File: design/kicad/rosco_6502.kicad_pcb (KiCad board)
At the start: 4 copper layers, 100 x 100 mm, 52 parts, among them IC1 W65C02SxP, IC2 ATF22V10C-7PX, IC3 XR68C681CJTR-F, IC4 NE555P, IC5 ATF22V10C-7PX, J1 UART_A, J2 UART_B, J3 Conn_01x06, J4 Conn_01x01_Male, J5 Conn_02x18_Odd_Even, Q1 3.6864MHz, SW1 SW_DPST, U1 AS6C4008-55PCN, U2 AS6C62256-55PCN, U3 AT28C64B-15PU, U4 74HCT174, X1 14MHz

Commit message: Tidy up some tracks
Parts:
- moved R10 1.33 mm to (98.5, 113.8)
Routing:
- net A12: track 181.7 -> 191.3 mm
- net Net-(IC3-Pad16): track 39.5 -> 46.9 mm
- net Net-(IC3-Pad15): track 48.6 -> 53.9 mm
- net CLK: track 161.8 -> 166.7 mm
- net A8: track 181.1 -> 185.7 mm
- net A13: track 162.7 -> 167.3 mm
- net A14: track 101.4 -> 105.9 mm
- net D2: track 180.4 -> 184.1 mm
- net ~{RESET}: track 235.7 -> 239.3 mm
- net A11: track 172.9 -> 175.0 mm
- net RDY: track 182.5 -> 184.1 mm
- net ~{DUASEL}: track 50.1 -> 48.9 mm
- net D4: track 130.3 -> 131.2 mm
- net D6: track 126.4 -> 127.4 mm
- net D7: track 133.7 -> 132.9 mm
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
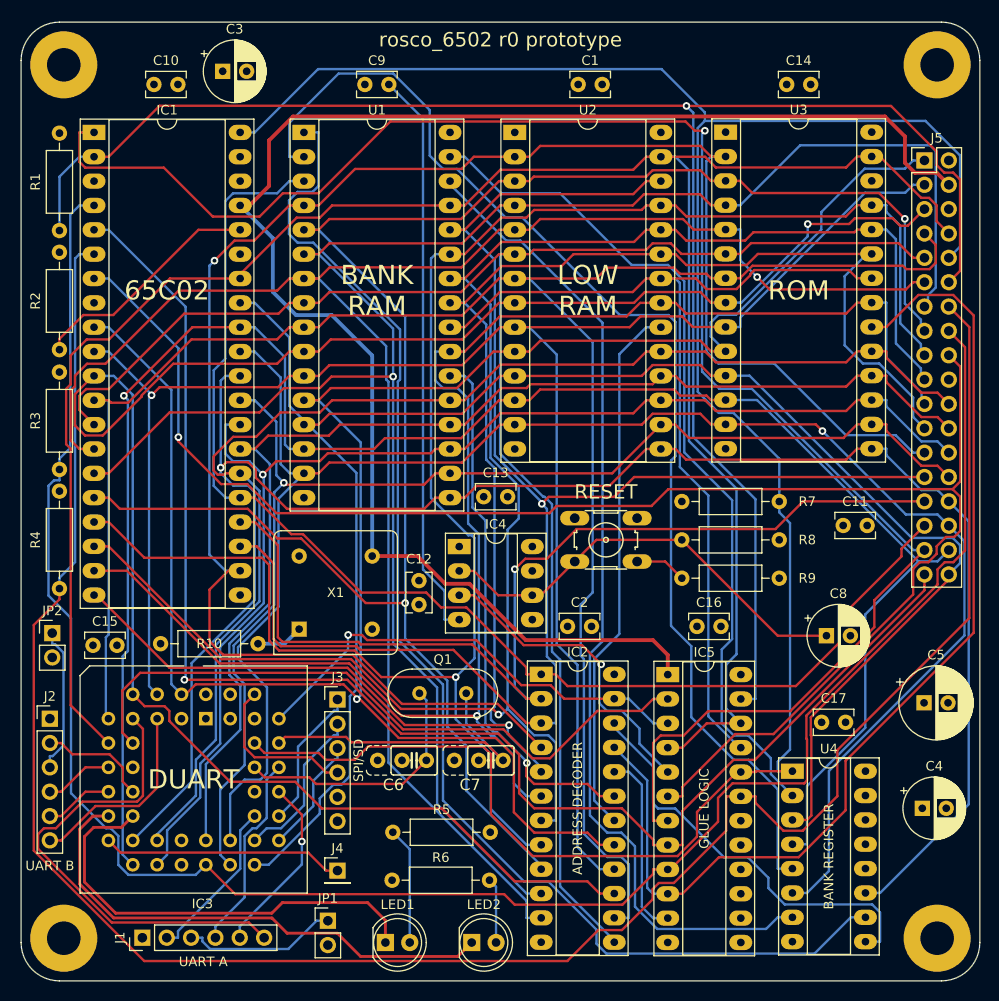
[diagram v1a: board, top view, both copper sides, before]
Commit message: Power connector & silk update
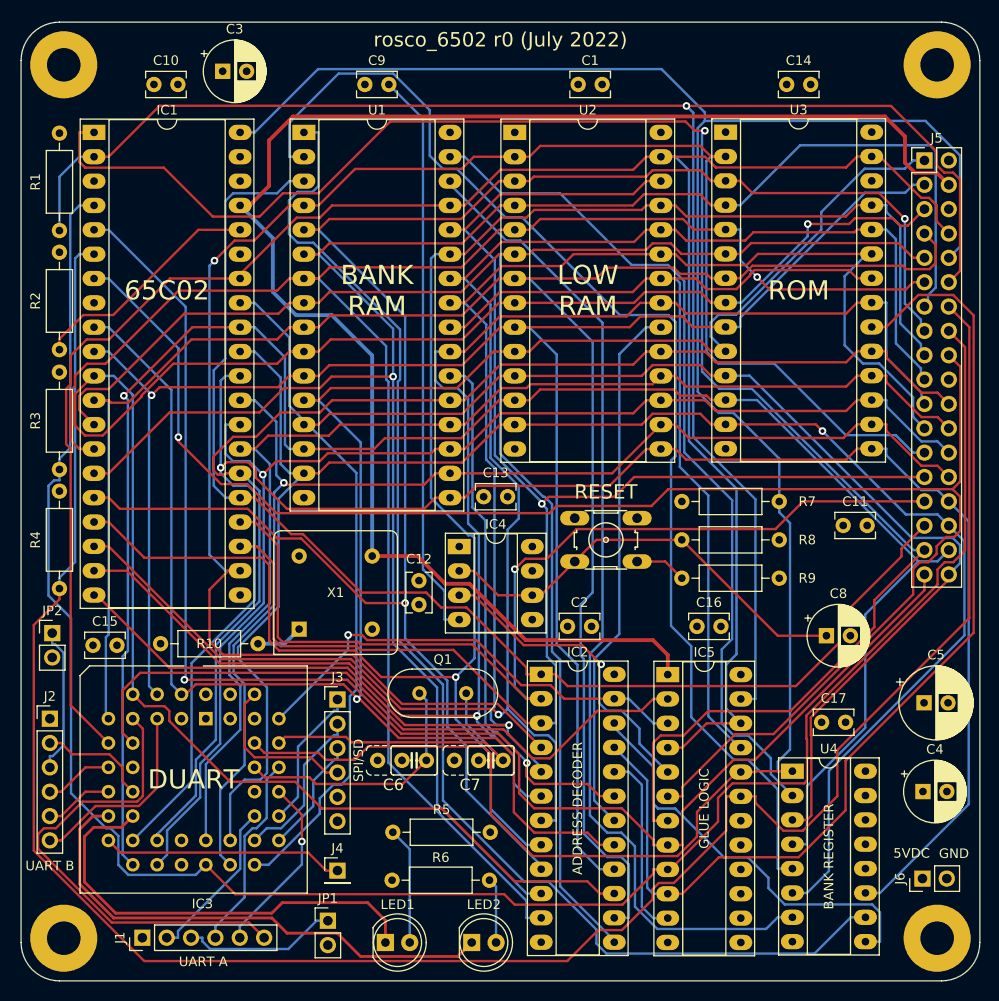
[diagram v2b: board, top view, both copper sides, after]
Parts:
- added J6: Conn_01x02_Male, Connector_PinHeader_2.54mm:PinHeader_1x02_P2.54mm_Vertical, F.Cu at (178.0, 138.3)
- moved C4 1.75 mm to (178.1, 129.2)
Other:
- board text added: "5VDC"
- board text added: "GND"
- board text added: "rosco_6502 r0 (July 2022)"
- board text removed: "rosco_6502 r0 prototype"
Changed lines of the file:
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@@
   )
   (paper "A4")
+  (title_block
+    (title "rosco_6502")
+    (date "2022-06-19")
+    (rev "0")
+    (company "The Really Old-School Company Limited")
+    (comment 1 "Copyright (c)2022 Ross Bamford & Contributors")
+    (comment 2 "Open Source Hardware (CERN OHL)")
+  )
   (layers
     (0 "F.Cu" signal)
@@
       (outputformat 1)
       (mirror false)
-      (drillshape 1)
+      (drillshape 0)
       (scaleselection 1)
-      (outputdirectory "")
+      (outputdirectory "../CAMOutputs/")
     )
   )
@@
   )
   (footprint "Capacitor_THT:CP_Radial_D6.3mm_P2.50mm" (layer "F.Cu")
-    (at 178 131)
+    (at 178.067621 129.25)
     (descr "CP, Radial series, Radial, pin pitch=2.50mm, , diameter=6.3mm, Electrolytic Capacitor")
     (tags "CP Radial series Radial pin pitch 2.50mm  diameter 6.3mm Electrolytic Capacitor")
@@
     )
   )
+  (footprint "Connector_PinHeader_2.54mm:PinHeader_1x02_P2.54mm_Vertical" (layer "F.Cu")
+    (at 178.015 138.33 90)
+    (descr "Through hole straight pin header, 1x02, 2.54mm pitch, single row")
+    (tags "Through hole pin header THT 1x02 2.54mm single row")
+    (property "Sheetfile" "rosco_6502.kicad_sch")
+    (property "Sheetname" "")
+    (attr through_hole)
+    (fp_text reference "J6" (at 0 -2.33 90) (layer "F.SilkS")
+      (effects (font (size 1 1) (thickness 0.15)))
+    )
+    (fp_text value "Conn_01x02_Male" (at 0 4.87 90) (layer "F.Fab")
+      (effects (font (size 1 1) (thickness 0.15)))
+    )
+    (fp_text user "${REFERENCE}" (at 0 1.27) (layer "F.Fab")
+      (effects (font (size 1 1) (thickness 0.15)))
+    )
+    (fp_line (start -1.33 3.87) (end 1.33 3.87) (layer "F.SilkS") (width 0.12))
+    (fp_line (start 1.33 1.27) (end 1.33 3.87) (layer "F.SilkS") (width 0.12))
+    (fp_line (start -1.33 1.27) (end -1.33 3.87) (layer "F.SilkS") (width 0.12))
+    (fp_line (start -1.33 -1.33) (end 0 -1.33) (layer "F.SilkS") (width 0.12))
+    (fp_line (start -1.33 1.27) (end 1.33 1.27) (layer "F.SilkS") (width 0.12))
+    (fp_line (start -1.33 0) (end -1.33 -1.33) (layer "F.SilkS") (width 0.12))
+    (fp_line (start -1.8 -1.8) (end -1.8 4.35) (layer "F.CrtYd") (width 0.05))
+    (fp_line (start 1.8 4.35) (end 1.8 -1.8) (layer "F.CrtYd") (width 0.05))
+    (fp_line (start -1.8 4.35) (end 1.8 4.35) (layer "F.CrtYd") (width 0.05))
+    (fp_line (start 1.8 -1.8) (end -1.8 -1.8) (layer "F.CrtYd") (width 0.05))
+    (fp_line (start 1.27 -1.27) (end 1.27 3.81) (layer "F.Fab") (width 0.1))
+    (fp_line (start 1.27 3.81) (end -1.27 3.81) (layer "F.Fab") (width 0.1))
+    (fp_line (start -1.27 -0.635) (end -0.635 -1.27) (layer "F.Fab") (width 0.1))
+    (fp_line (start -0.635 -1.27) (end 1.27 -1.27) (layer "F.Fab") (width 0.1))
+    (fp_line (start -1.27 3.81) (end -1.27 -0.635) (layer "F.Fab") (width 0.1))
+    (pad "1" thru_hole rect locked (at 0 0 90) (size 1.7 1.7) (drill 1) (layers *.Cu *.Mask)
+      (net 2 "VCC") (pinfunction "Pin_1") (pintype "passive"))
+    (pad "2" thru_hole oval locked (at 0 2.54 90) (size 1.7 1.7) (drill 1) (layers *.Cu *.Mask)
+      (net 1 "GND") (pinfunction "Pin_2") (pintype "passive"))
+    (model "${KICAD6_3DMODEL_DIR}/Connector_PinHeader_2.54mm.3dshapes/PinHeader_1x02_P2.54mm_Vertical.wrl"
+      (offset (xyz 0 0 0))
+      (scale (xyz 1 1 1))
+      (rotate (xyz 0 0 0))
+    )
+  )
   (footprint "Package_DIP:DIP-40_W15.24mm_Socket_LongPads" (layer "F.Cu")
     (at 91.6083 60.5)
@@
     (effects (font (size 1.5 1.5) (thickness 0.3)) (justify mirror))
   )
+  (gr_text "5VDC" (at 176.885238 135.69) (layer "F.SilkS")
+    (effects (font (size 1 1) (thickness 0.15)))
+  )
   (gr_text "ROM" (at 165.1083 77) (layer "F.SilkS")
     (effects (font (size 2 2) (thickness 0.3)))
@@
     (effects (font (size 2 2) (thickness 0.3)))
   )
-  (gr_text "rosco_6502 r0 prototype" (at 134 50.84) (layer "F.SilkS")
+  (gr_text "rosco_6502 r0 (July 2022)" (at 134 50.84) (layer "F.SilkS")
     (effects (font (size 1.5 1.5) (thickness 0.3)))
   )
@@
     (effects (font (size 1 1) (thickness 0.15)))
   )
+  (gr_text "GND" (at 181.303809 135.72) (layer "F.SilkS")
+    (effects (font (size 1 1) (thickness 0.15)))
+  )

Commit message: Add CLK into RD/WR and reroute
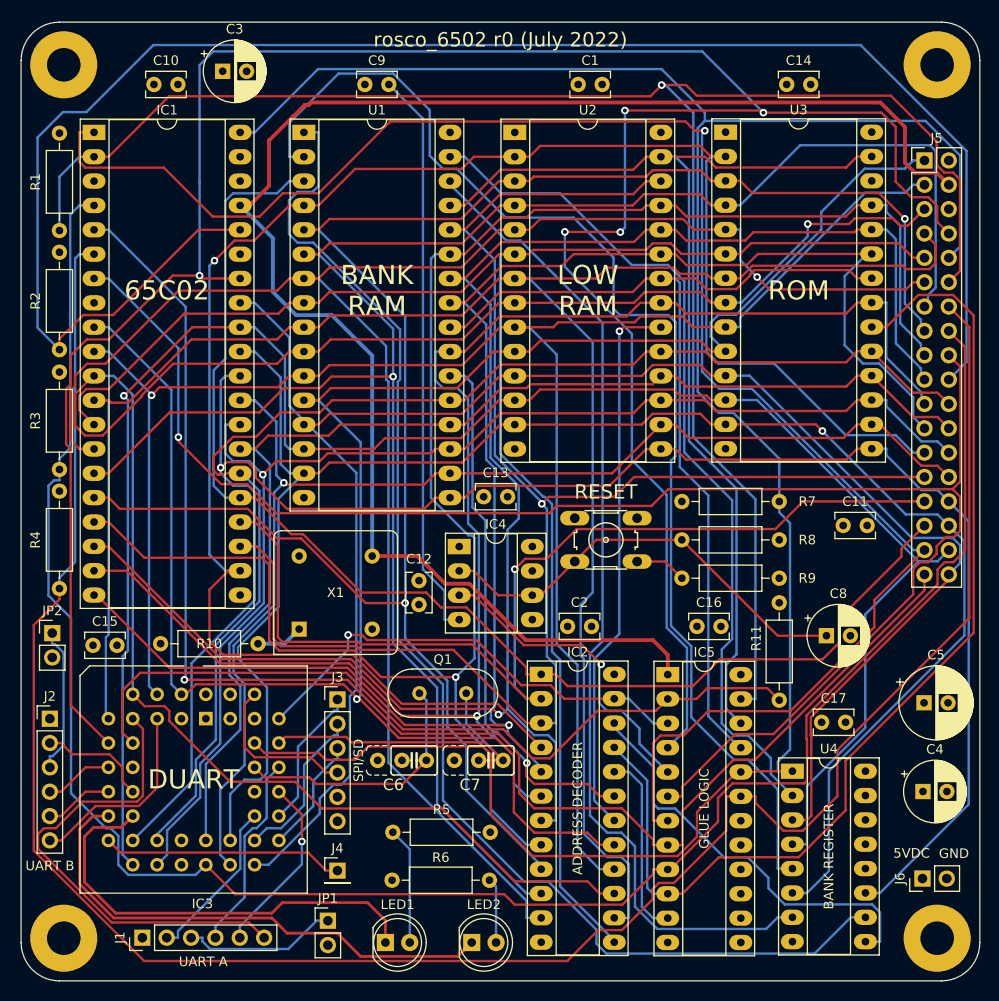
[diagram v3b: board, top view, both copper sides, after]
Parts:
- added R11: 3K3, Resistor_THT:R_Axial_DIN0207_L6.3mm_D2.5mm_P10.16mm_Horizontal, F.Cu at (163.1, 109.6)
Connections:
- net W/~{R} renamed ~{RD}
- IC1 pad 36: Net-(IC1-Pad36) -> BE
- IC5 pad 22: R/~{W} -> ~{WR}
- R2 pad 2: Net-(IC1-Pad36) -> BE
- U1 pad 29: R/~{W} -> ~{WR}
- U2 pad 27: R/~{W} -> ~{WR}
- U3 pad 27: R/~{W} -> ~{WR}
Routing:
- net BE: track 0.00 -> 177.8 mm
- net ~{WR}: track 0.00 -> 110.2 mm
- net R/~{W}: track 221.1 -> 269.7 mm, vias 0 -> 5
- net Net-(IC1-Pad36): track 24.7 -> 0.00 mm
- net ~{DUADTACK}: track 69.8 -> 82.4 mm
- net RDY: track 184.1 -> 190.1 mm
- net BANK1: track 125.2 -> 128.3 mm
- net D4: track 131.2 -> 129.2 mm
- net A11: track 175.0 -> 173.0 mm
- net D7: track 132.9 -> 131.3 mm
- net A7: track 194.7 -> 193.1 mm
- net ~{LOWRAM}: track 56.1 -> 57.5 mm, vias 0 -> 1
- net D5: track 133.1 -> 131.9 mm
- net D0: track 186.3 -> 185.4 mm
- net Net-(C8-Pad1): track 45.9 -> 45.0 mm
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
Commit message: Fix incorrect 555 hookup
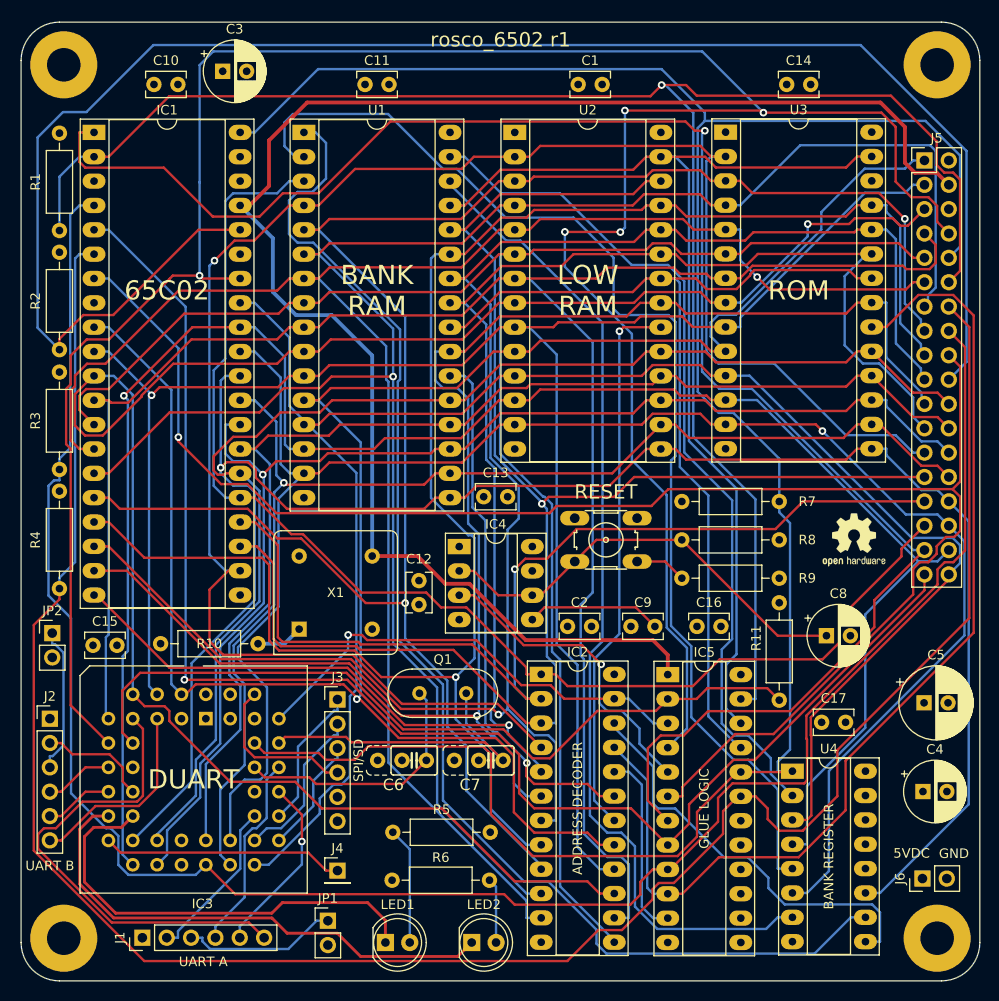
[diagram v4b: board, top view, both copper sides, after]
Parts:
- added REF**: OSHW-Logo2_7.3x6mm_SilkScreen, Symbol:OSHW-Logo2_7.3x6mm_SilkScreen, F.Cu at (170.9, 103.0)
- moved C11 67.8 mm to (119.9, 55.5)
- moved C9 63.0 mm to (147.6, 112.0)
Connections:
- C9 pad 2: Net-(C9-Pad2) -> Net-(IC4-Pad5)
- IC4 pad 4: Net-(C9-Pad2) -> VCC
- IC4 pad 5: VCC -> Net-(IC4-Pad5)
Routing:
- net Net-(C9-Pad2): track 59.8 -> 0.00 mm
- net Net-(IC4-Pad5): track 0.00 -> 14.1 mm
- net BANK1: track 128.3 -> 122.4 mm
- net ~{ML}: track 153.3 -> 152.4 mm
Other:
- board text added: "rosco_6502 r1"
- board text removed: "rosco_6502 r0 (July 2022)"

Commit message: Fix incorrect button symbol
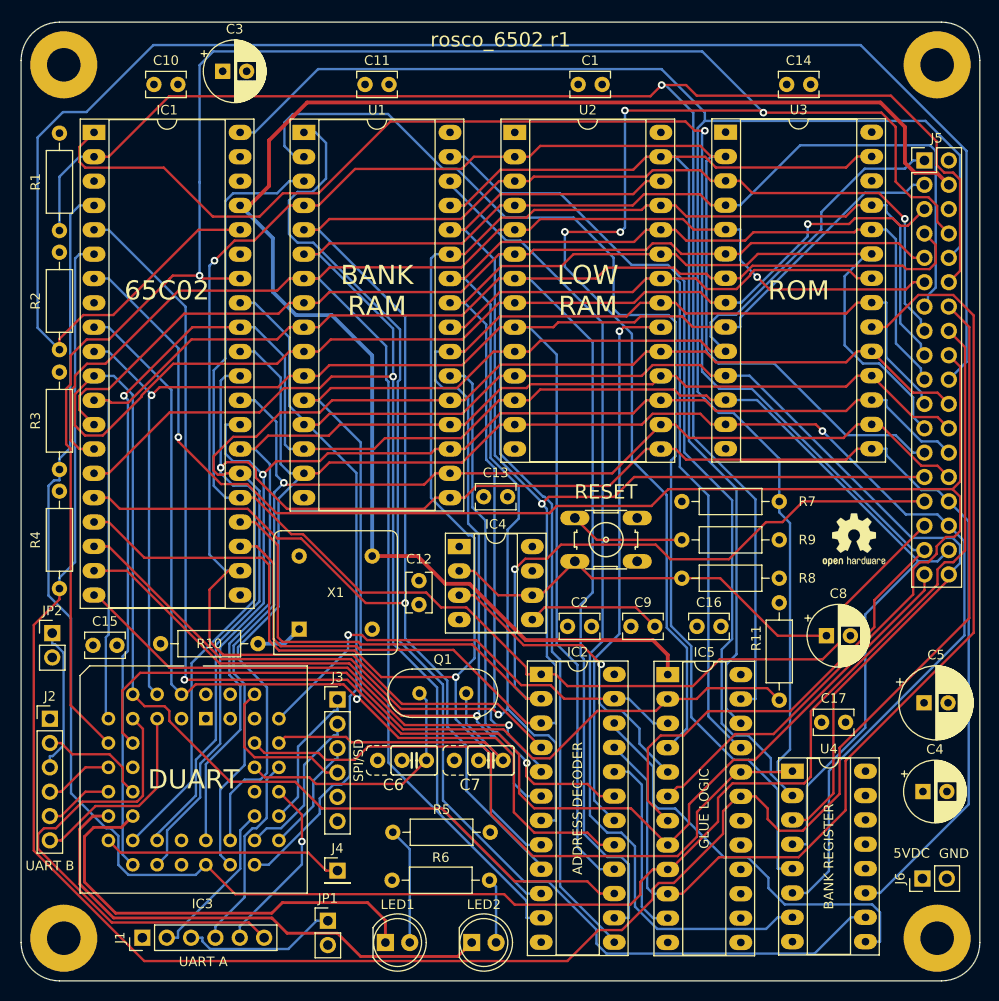
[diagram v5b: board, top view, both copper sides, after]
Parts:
- removed SW1: SW_DPST, rosco_6502:B3F-10XX
- added S1: 10-XX, rosco_6502:B3F-10XX, F.Cu at (145.0, 103.0)
- moved R8 4.00 mm to (152.9, 107.0)
- moved R9 4.00 mm to (152.9, 103.0)
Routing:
- net Net-(R9-Pad1): track 5.39 -> 12.1 mm
- net Net-(C8-Pad1): track 45.0 -> 43.1 mm
- net A14: track 105.9 -> 107.1 mm
- net ~{VP}: track 180.3 -> 179.4 mm
- net SYNC: track 170.5 -> 169.9 mm
